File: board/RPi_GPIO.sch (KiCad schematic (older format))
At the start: 41 parts, among them IC1 ATMEGA328-A, IC2 RFM69HW, J1 RPi_GPIO, P1 FTDI_CONN_01X06, P10 SW_CONN, P11 BATT_IN, P12 CONN_01X01, P13 ICSP, P2 D8, P3 A0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

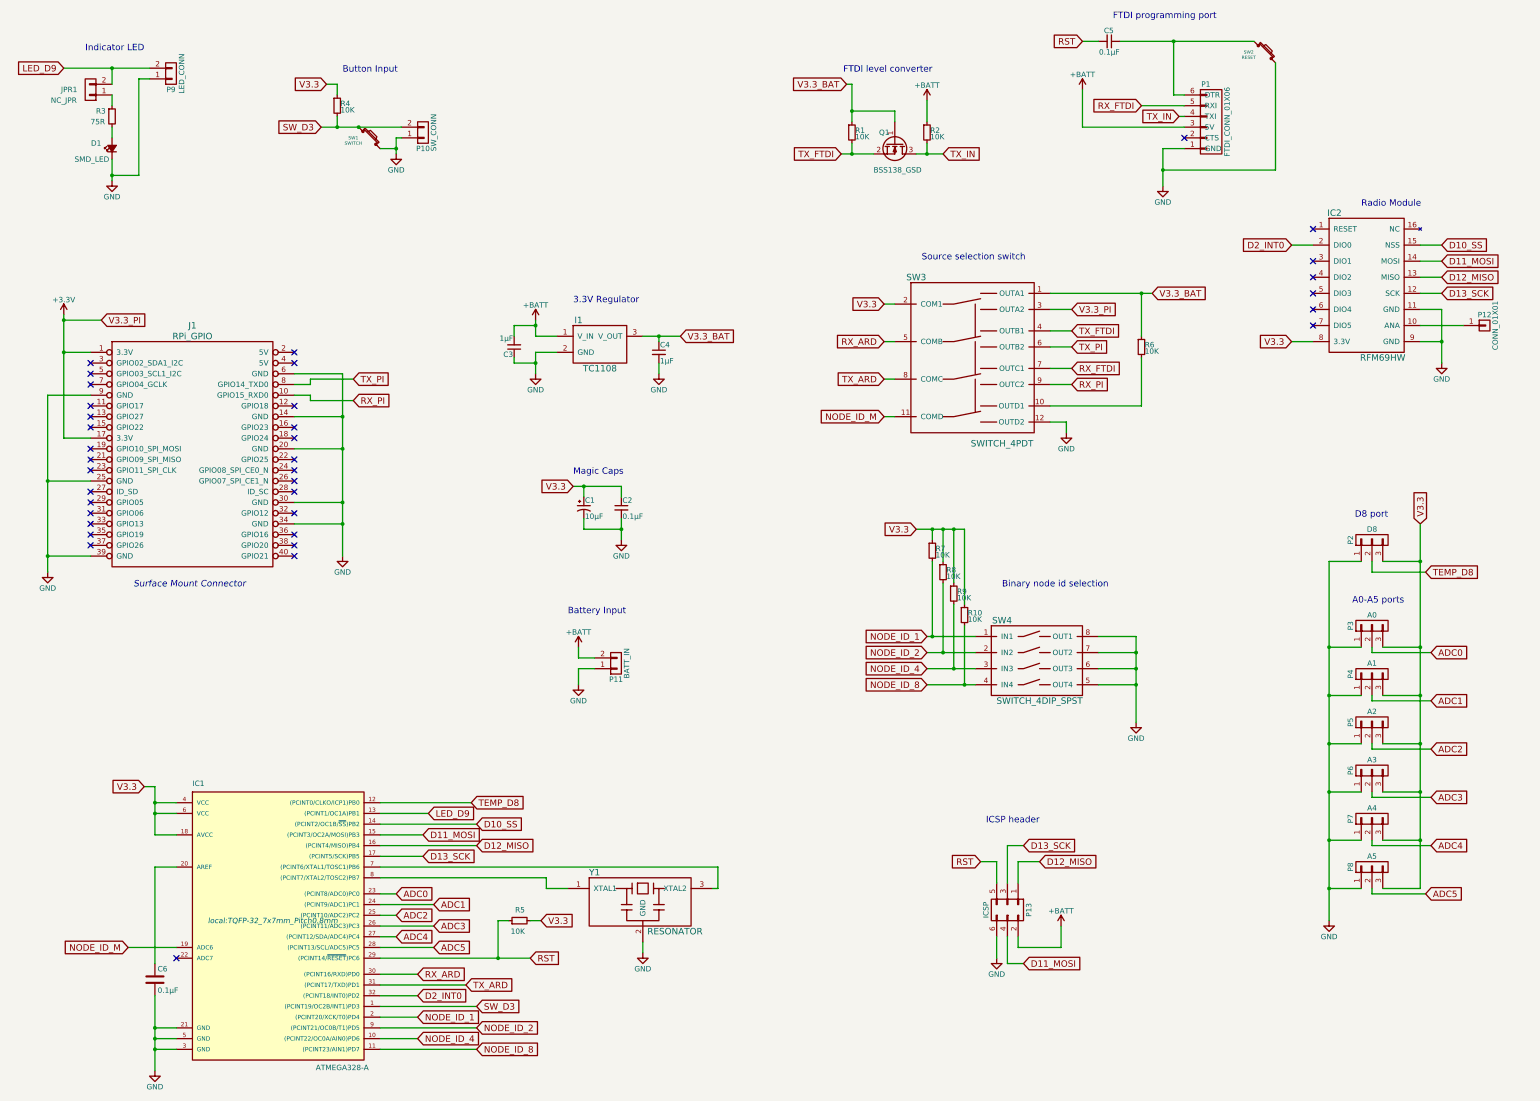
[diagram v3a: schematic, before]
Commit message: schematic and netlist changes for issues 1–5
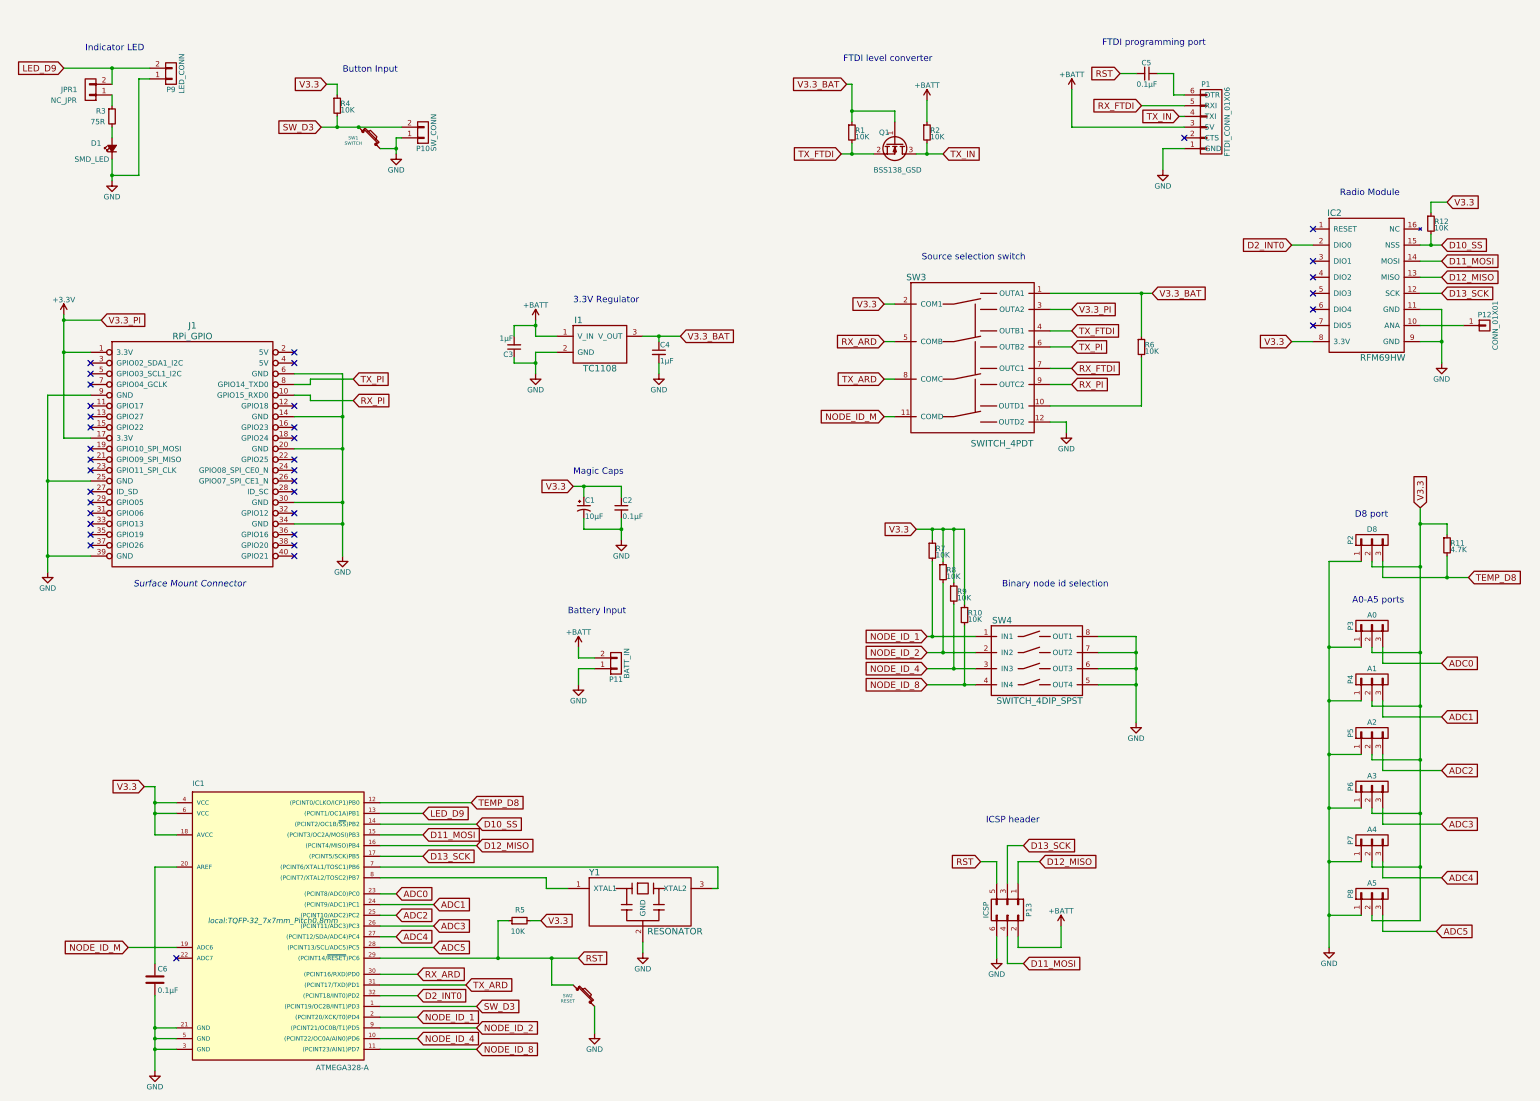
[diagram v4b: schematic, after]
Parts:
- added R11: 4.7K, Resistors_SMD:R_0603_HandSoldering, symbol R_Small
- added R12: 10K, Resistors_SMD:R_0603_HandSoldering, symbol R_Small
- I1: footprint TO_SOT_Packages_SMD:SOT-23_Handsoldering -> TO_SOT_Packages_SMD:SOT-223
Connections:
- net ADC0: now also P3.3 (P3); no longer P3.2 (P2)
- net ADC1: now also P4.3 (P3); no longer P4.2 (P2)
- net ADC2: now also P5.3 (P3); no longer P5.2 (P2)
- net ADC3: now also P6.3 (P3); no longer P6.2 (P2)
- net ADC4: now also P7.3 (P3); no longer P7.2 (P2)
- net ADC5: now also P8.3 (P3); no longer P8.2 (P2)
- net D10_SS: now also R12.2
- net RST: now also SW2.1
- net TEMP_D8: now also P2.3 (P3), R11.2; no longer P2.2 (P2)
- net V3.3: now also P2.2 (P2), P3.2 (P2), P4.2 (P2), P5.2 (P2), P6.2 (P2), P7.2 (P2), P8.2 (P2), R11.1, R12.1; no longer P2.3 (P3), P3.3 (P3), P4.3 (P3), P5.3 (P3), P6.3 (P3), P7.3 (P3), P8.3 (P3)
- net at C5.1, P1.6 (DTR): no longer SW2.1
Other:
- moved on the sheet: C5, P4, P5, P6, P7, P8, SW2
